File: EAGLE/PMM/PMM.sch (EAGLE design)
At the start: 19 parts, among them J1 TB001-500-12BE, K1 EC2-5NU, K2 G6DN-1A_DC5, K3 35701331, K4 35701331

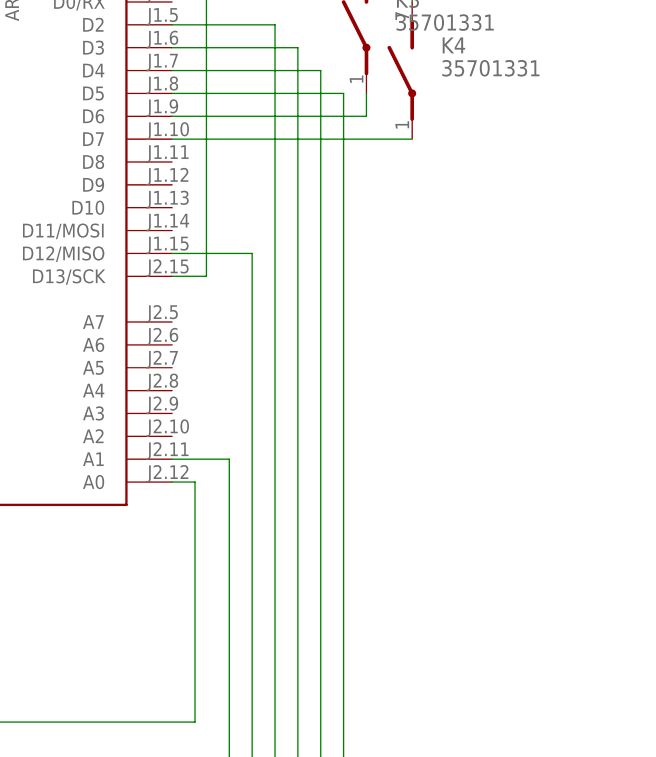
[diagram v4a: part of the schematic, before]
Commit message: Added indicator LEDs
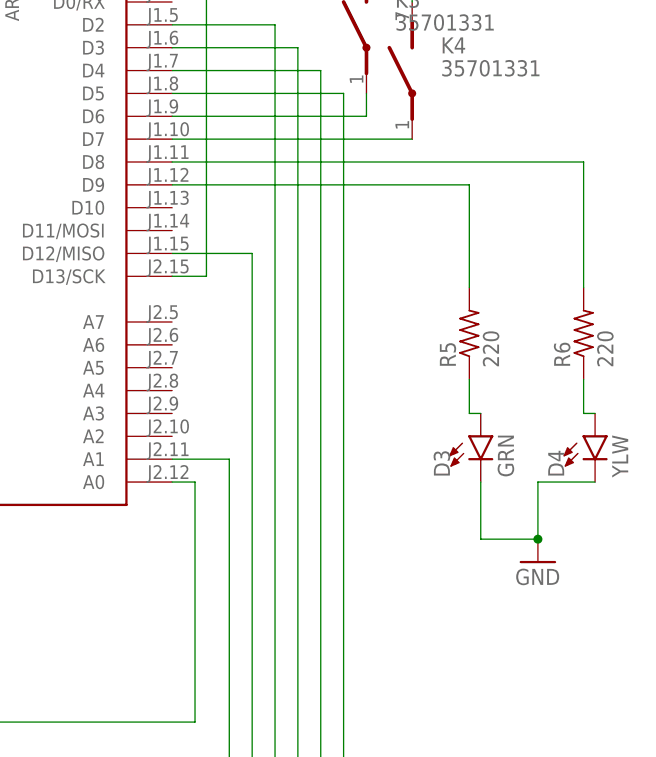
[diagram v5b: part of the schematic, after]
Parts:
- added D3: GRN, SparkFun-LED:LED5MM-KIT
- added D4: YLW, SparkFun-LED:LED5MM-KIT
- added R5, R6: 220, adafruit:R-US_0207/12
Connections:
- new net N$23: D3.A, R5.1
- new net N$24: MODUL1.D8, R6.2
- new net N$25: MODUL1.D9, R5.2
- new net N$6: D4.A, R6.1
- net GND: now also D3.C, D4.C
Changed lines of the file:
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@@
 <layer number="112" name="tSilk" color="7" fill="1" visible="no" active="yes"/>
 <layer number="113" name="ReferenceLS" color="7" fill="1" visible="no" active="no"/>
+<layer number="114" name="Badge_Outline" color="7" fill="1" visible="no" active="no"/>
+<layer number="115" name="ReferenceISLANDS" color="7" fill="1" visible="no" active="no"/>
 <layer number="116" name="Patch_BOT" color="9" fill="4" visible="no" active="yes"/>
 <layer number="118" name="Rect_Pads" color="7" fill="1" visible="no" active="no"/>
@@
 <part name="K3" library="relay" library_urn="urn:adsk.eagle:library:339" deviceset="35701331" device="" package3d_urn="urn:adsk.eagle:package:24297/1"/>
 <part name="K4" library="relay" library_urn="urn:adsk.eagle:library:339" deviceset="35701331" device="" package3d_urn="urn:adsk.eagle:package:24297/1"/>
+<part name="D3" library="SparkFun-LED" deviceset="LED" device="5MM-KIT" value="GRN"/>
+<part name="D4" library="SparkFun-LED" deviceset="LED" device="5MM-KIT" value="YLW"/>
+<part name="R5" library="adafruit" library_urn="urn:adsk.eagle:library:420" deviceset="R-US_" device="0207/12" package3d_urn="urn:adsk.eagle:package:6240598/1" value="220"/>
+<part name="R6" library="adafruit" library_urn="urn:adsk.eagle:library:420" deviceset="R-US_" device="0207/12" package3d_urn="urn:adsk.eagle:package:6240598/1" value="220"/>
+<part name="GND8" library="supply1" library_urn="urn:adsk.eagle:library:371" deviceset="GND" device=""/>
 </parts>
 <sheets>
@@
 <attribute name="PART" x="160.655" y="70.485" size="1.778" layer="95"/>
 <attribute name="VALUE" x="160.655" y="67.945" size="1.778" layer="96"/>
+</instance>
+<instance part="D3" gate="D1" x="165.1" y="27.94" smashed="yes">
+<attribute name="NAME" x="161.671" y="23.368" size="1.778" layer="95" font="vector" rot="R90"/>
+<attribute name="VALUE" x="167.005" y="23.368" size="1.778" layer="96" font="vector" rot="R90" align="top-left"/>
+</instance>
+<instance part="D4" gate="D1" x="177.8" y="27.94" smashed="yes">
+<attribute name="NAME" x="174.371" y="23.368" size="1.778" layer="95" font="vector" rot="R90"/>
+<attribute name="VALUE" x="179.705" y="23.368" size="1.778" layer="96" font="vector" rot="R90" align="top-left"/>
+</instance>
+<instance part="R5" gate="G$1" x="163.83" y="39.37" smashed="yes" rot="R90">
+<attribute name="NAME" x="162.3314" y="35.56" size="1.778" layer="95" rot="R90"/>
+<attribute name="VALUE" x="167.132" y="35.56" size="1.778" layer="96" rot="R90"/>
+</instance>
+<instance part="R6" gate="G$1" x="176.53" y="39.37" smashed="yes" rot="R90">
+<attribute name="NAME" x="175.0314" y="35.56" size="1.778" layer="95" rot="R90"/>
+<attribute name="VALUE" x="179.832" y="35.56" size="1.778" layer="96" rot="R90"/>
+</instance>
+<instance part="GND8" gate="1" x="171.45" y="13.97" smashed="yes">
+<attribute name="VALUE" x="168.91" y="11.43" size="1.778" layer="96"/>
 </instance>
 </instances>
@@
 <junction x="102.87" y="8.89"/>
 </segment>
+<segment>
+<pinref part="GND8" gate="1" pin="GND"/>
+<pinref part="D3" gate="D1" pin="C"/>
+<wire x1="171.45" y1="16.51" x2="165.1" y2="16.51" width="0.1524" layer="91"/>
+<wire x1="165.1" y1="16.51" x2="165.1" y2="22.86" width="0.1524" layer="91"/>
+<pinref part="D4" gate="D1" pin="C"/>
+<wire x1="177.8" y1="22.86" x2="171.45" y2="22.86" width="0.1524" layer="91"/>
+<wire x1="171.45" y1="22.86" x2="171.45" y2="16.51" width="0.1524" layer="91"/>
+<junction x="171.45" y="16.51"/>
+</segment>
 </net>
 <net name="N$10" class="0">
@@
 </segment>
 </net>
+<net name="N$6" class="0">
+<segment>
+<pinref part="R6" gate="G$1" pin="1"/>
+<pinref part="D4" gate="D1" pin="A"/>
+<wire x1="176.53" y1="34.29" x2="176.53" y2="30.48" width="0.1524" layer="91"/>
+<wire x1="176.53" y1="30.48" x2="177.8" y2="30.48" width="0.1524" layer="91"/>
+</segment>
+</net>
+<net name="N$23" class="0">
+<segment>
+<pinref part="R5" gate="G$1" pin="1"/>
+<pinref part="D3" gate="D1" pin="A"/>
+<wire x1="163.83" y1="34.29" x2="163.83" y2="30.48" width="0.1524" layer="91"/>
+<wire x1="163.83" y1="30.48" x2="165.1" y2="30.48" width="0.1524" layer="91"/>
+</segment>
+</net>
+<net name="N$24" class="0">
+<segment>
+<pinref part="R6" gate="G$1" pin="2"/>
+<pinref part="MODUL1" gate="MODUL" pin="D8"/>
+<wire x1="176.53" y1="44.45" x2="176.53" y2="58.42" width="0.1524" layer="91"/>
+<wire x1="176.53" y1="58.42" x2="130.81" y2="58.42" width="0.1524" layer="91"/>
+</segment>
+</net>
+<net name="N$25" class="0">
+<segment>
+<pinref part="R5" gate="G$1" pin="2"/>
+<pinref part="MODUL1" gate="MODUL" pin="D9"/>
+<wire x1="163.83" y1="44.45" x2="163.83" y2="55.88" width="0.1524" layer="91"/>
+<wire x1="163.83" y1="55.88" x2="130.81" y2="55.88" width="0.1524" layer="91"/>
+</segment>
+</net>

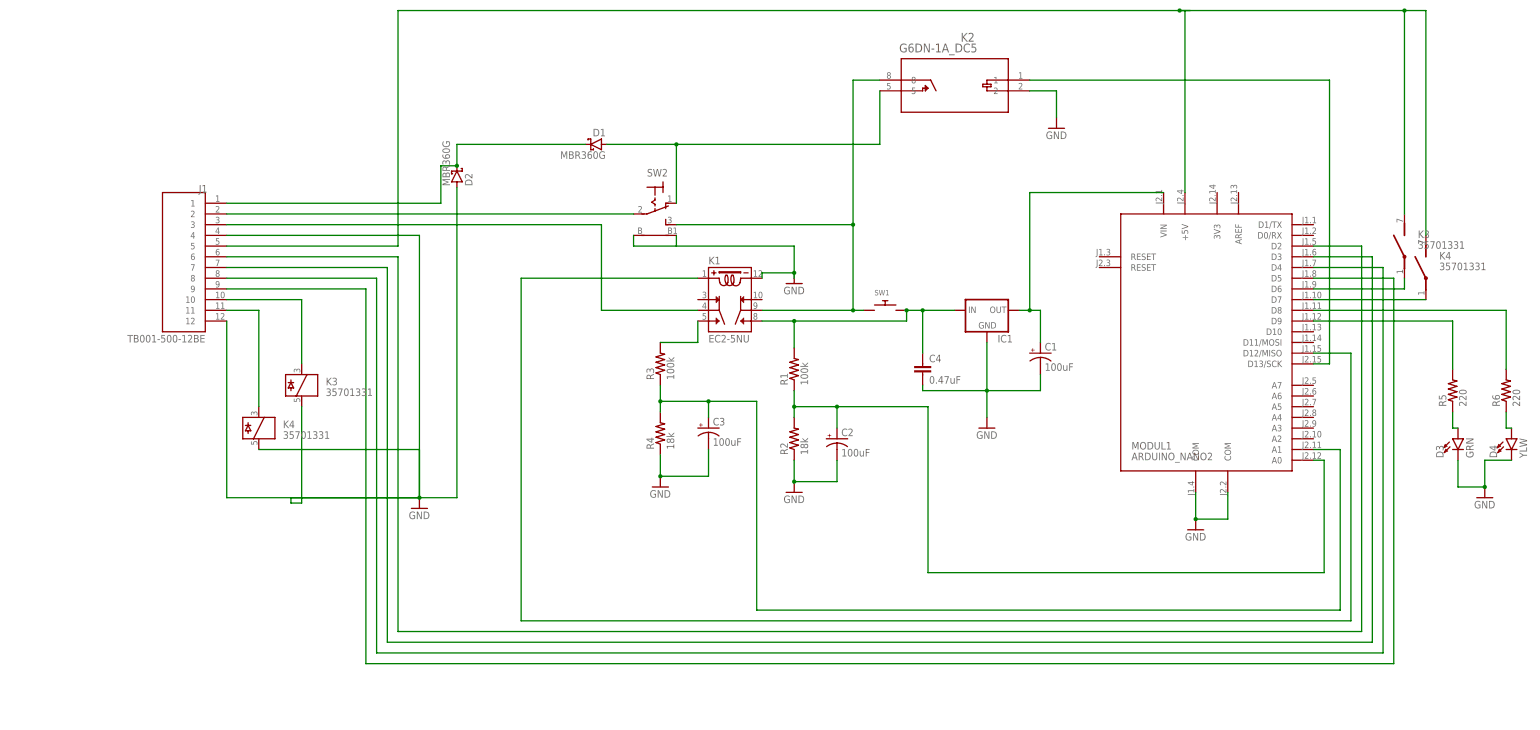
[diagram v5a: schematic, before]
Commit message: Changed spare DIO to 2 in, 2 out, all relay isolated
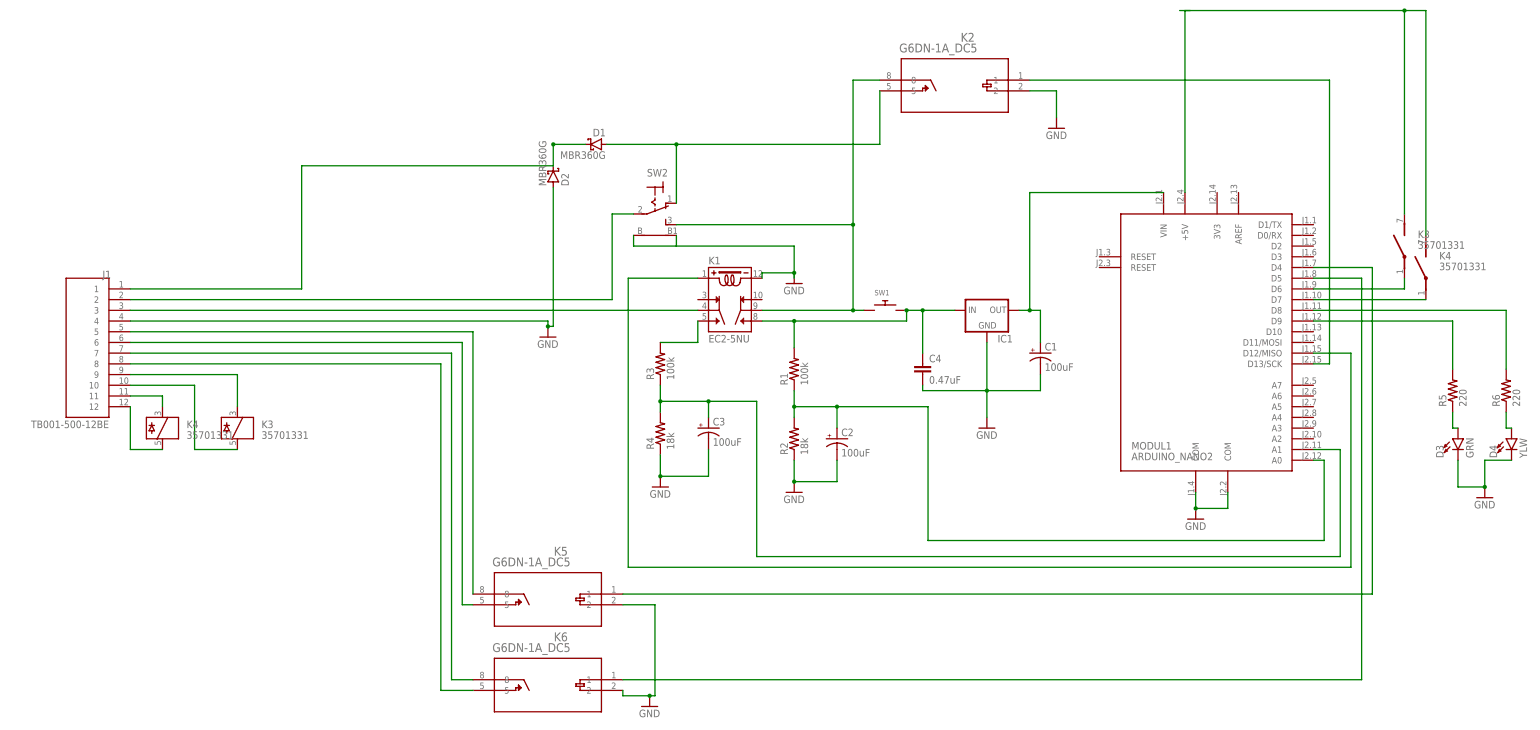
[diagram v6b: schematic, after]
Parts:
- added K5, K6: G6DN-1A_DC5, G6DN:G6DN-1A_DC5
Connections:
- new net N$26: J1.5, K5.8
- new net N$27: J1.6, K5.5
- new net N$28: J1.7, K6.8
- new net N$29: J1.8, K6.5
- net GND: now also K5.2, K6.2; no longer J1.12, K31.5, K41.5
- net N$13: no longer J1.5
- net N$14: now also J1.9, K31.3; no longer J1.6, MODUL1.D2
- net N$15: now also J1.12, K41.5; no longer J1.7, MODUL1.D3
- net N$16: now also J1.10, K31.5; no longer J1.8, MODUL1.D4
- net N$17: now also K6.1; no longer J1.9
- net N$18: now also K5.1, MODUL1.D4; no longer J1.10, K31.3
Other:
- moved on the sheet: D2, J1, K3, K4
